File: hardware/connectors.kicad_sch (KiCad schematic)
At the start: 14 parts, among them J2 USB_C_Receptacle_USB2.0_16P, J3 Conn_01x03

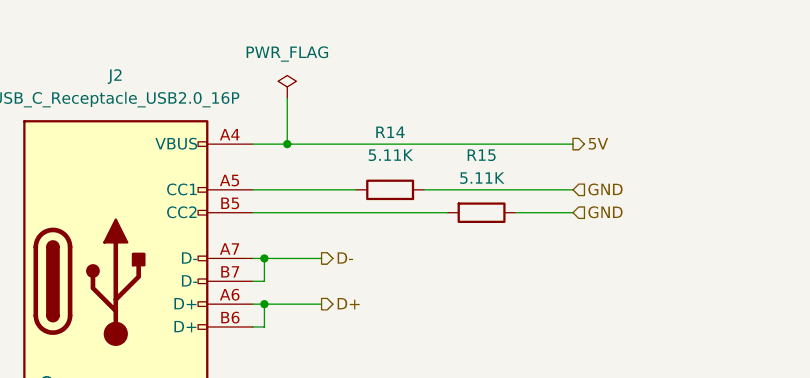
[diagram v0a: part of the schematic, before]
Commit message: Fix most of ERC on schema. Add missing wire on RV1. Add PWR_FLG on GND to avoid error. Add resistor for unused SPI_OUT of HV5622. Add PTC on 3v3 supply.
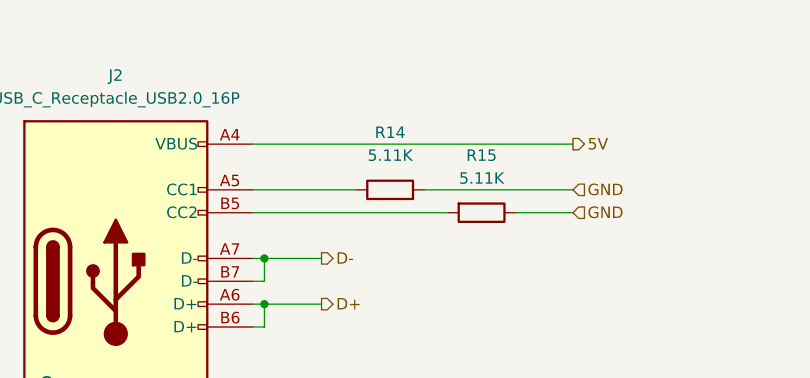
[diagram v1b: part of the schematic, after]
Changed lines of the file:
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@@
-	)
-	(junction
-		(at 80.01 44.45)
-		(diameter 0)
-		(color 0 0 0 0)
 	)
 	(junction
@@
 	(wire
 		(pts
-			(xy 80.01 39.37) (xy 80.01 44.45)
-		)
-		(stroke
-			(width 0)
-			(type default)
-		)
-	)
-	(wire
-		(pts
 			(xy 95.25 49.53) (xy 111.76 49.53)
 		)
@@
 	(wire
 		(pts
-			(xy 80.01 44.45) (xy 111.76 44.45)
+			(xy 76.2 44.45) (xy 111.76 44.45)
 		)
 		(stroke
@@
 		(pts
 			(xy 78.74 74.93) (xy 78.74 77.47)
-		)
-		(stroke
-			(width 0)
-			(type default)
-		)
-	)
-	(wire
-		(pts
-			(xy 76.2 44.45) (xy 80.01 44.45)
 		)
 		(stroke
@@
 					(unit 1)
 				)
-			)
-		)
-	)
-	(symbol
-		(lib_id "power:PWR_FLAG")
-		(at 80.01 39.37 0)
-		(unit 1)
-		(exclude_from_sim no)
-		(in_bom yes)
-		(on_board yes)
-		(dnp no)
-		(fields_autoplaced yes)
-		(property "Reference" "#FLG04"
-			(at 80.01 37.465 0)
-			(effects
-				(font
-					(size 1.27 1.27)
-				)
-				(hide yes)
-			)
-		)
-		(property "Value" "PWR_FLAG"
-			(at 80.01 34.29 0)
-			(effects
-				(font
-					(size 1.27 1.27)
-				)
-			)
-		)
-		(property "Footprint" ""
-			(at 80.01 39.37 0)
-			(effects
-				(font
-					(size 1.27 1.27)
-				)
-				(hide yes)
-			)
-		)
-		(property "Datasheet" "~"
-			(at 80.01 39.37 0)
-			(effects
-				(font
-					(size 1.27 1.27)
-				)
-				(hide yes)
-			)
-		)
-		(property "Description" "Special symbol for telling ERC where power comes from"
-			(at 80.01 39.37 0)
-			(effects
-				(font
-					(size 1.27 1.27)
-				)
-				(hide yes)
-			)
-		)
-		(pin "1"
-		)
-		(instances
-			(project ""
-				(path "/90430e5f-7049-4de8-b92d-f897c4a89819/7e2fbc03-0d09-4c94-a49f-ff5156ee2f2b"
-					(reference "#FLG04")
-					(unit 1)
-				)

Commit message: Update PCB.
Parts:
- added TH1, TH2: Thermistor_PTC, Resistor_SMD:R_1206_3216Metric, symbol Device:Thermistor_PTC
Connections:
- net 12V: now also TH1.1; no longer J3.3 (Pin_3)
- net 5V: now also TH2.1; no longer J2.A4 (VBUS), J2.A9 (VBUS), J2.B4 (VBUS), J2.B9 (VBUS)
- new net: J3.3 (Pin_3), TH1.2
- new net: J2.A4 (VBUS), J2.A9 (VBUS), J2.B4 (VBUS), J2.B9 (VBUS), TH2.2
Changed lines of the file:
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@@
 	(wire
 		(pts
-			(xy 199.39 43.18) (xy 212.09 43.18)
+			(xy 209.55 43.18) (xy 212.09 43.18)
+		)
+		(stroke
+			(width 0)
+			(type default)
+		)
+	)
+	(wire
+		(pts
+			(xy 199.39 50.8) (xy 200.66 50.8)
 		)
 		(stroke
@@
 	(wire
 		(pts
-			(xy 168.91 38.1) (xy 177.8 38.1)
+			(xy 208.28 50.8) (xy 209.55 50.8)
+		)
+		(stroke
+			(width 0)
+			(type default)
+		)
+	)
+	(wire
+		(pts
+			(xy 152.4 40.64) (xy 173.99 40.64)
+		)
+		(stroke
+			(width 0)
+			(type default)
+		)
+	)
+	(wire
+		(pts
+			(xy 152.4 38.1) (xy 177.8 38.1)
 		)
 		(stroke
@@
 	(wire
 		(pts
-			(xy 168.91 40.64) (xy 173.99 40.64)
-		)
-		(stroke
-			(width 0)
-			(type default)
-		)
-	)
-	(wire
-		(pts
 			(xy 76.2 64.77) (xy 77.47 64.77)
 		)
@@
 	(wire
 		(pts
-			(xy 76.2 44.45) (xy 111.76 44.45)
-		)
-		(stroke
-			(width 0)
-			(type default)
-		)
-	)
-	(wire
-		(pts
 			(xy 77.47 64.77) (xy 77.47 62.23)
 		)
@@
 	(wire
 		(pts
-			(xy 199.39 40.64) (xy 199.39 43.18)
+			(xy 199.39 40.64) (xy 199.39 50.8)
 		)
 		(stroke
@@
 	(wire
 		(pts
+			(xy 76.2 44.45) (xy 101.6 44.45)
+		)
+		(stroke
+			(width 0)
+			(type default)
+		)
+	)
+	(wire
+		(pts
 			(xy 78.74 74.93) (xy 78.74 77.47)
 		)
@@
 	(wire
 		(pts
+			(xy 209.55 50.8) (xy 209.55 43.18)
+		)
+		(stroke
+			(width 0)
+			(type default)
+		)
+	)
+	(wire
+		(pts
 			(xy 45.72 129.54) (xy 76.2 129.54)
+		)
+		(stroke
+			(width 0)
+			(type default)
+		)
+	)
+	(wire
+		(pts
+			(xy 109.22 44.45) (xy 111.76 44.45)
 		)
 		(stroke
@@
 		)
 	)
+	(hierarchical_label "5V"
+		(shape output)
+		(at 111.76 44.45 0)
+		(effects
+			(font
+				(size 1.27 1.27)
+			)
+			(justify left)
+		)
+	)
 	(hierarchical_label "GND"
 		(shape input)
@@
 		)
 	)
-	(hierarchical_label "5V"
-		(shape output)
-		(at 111.76 44.45 0)
-		(effects
-			(font
-				(size 1.27 1.27)
-			)
-			(justify left)
-		)
-	)
 	(hierarchical_label "D-"
 		(shape output)
@@
 	(hierarchical_label "170V"
 		(shape output)
-		(at 168.91 38.1 180)
+		(at 152.4 38.1 180)
 		(effects
 			(font
@@
 	(hierarchical_label "12V"
 		(shape output)
-		(at 168.91 40.64 180)
+		(at 152.4 40.64 180)
 		(effects
 			(font
@@
 		(on_board yes)
 		(dnp no)
-		(fields_autoplaced yes)
 		(property "Reference" "R14"
-			(at 91.44 43.18 90)
+			(at 91.44 47.244 90)
 			(effects
 				(font
@@
 		)
 		(property "Value" "5.11K"
-			(at 91.44 45.72 90)
+			(at 97.282 47.244 90)
 			(effects
 				(font
@@
 	)
 	(symbol
+		(lib_id "Device:Thermistor_PTC")
+		(at 105.41 44.45 270)
+		(unit 1)
+		(exclude_from_sim no)
+		(in_bom yes)
+		(on_board yes)
+		(dnp no)
+		(property "Reference" "TH2"
+			(at 105.41 39.878 90)
+			(effects
+				(font
+					(size 1.27 1.27)
+				)
+				(justify right)
+			)
+		)
+		(property "Value" "Thermistor_PTC"
+			(at 116.332 37.084 90)
+			(effects
+				(font
+					(size 1.27 1.27)
+				)
+				(justify right)
+			)
+		)
+		(property "Footprint" "Resistor_SMD:R_1206_3216Metric"
+			(at 100.33 45.72 0)
+			(effects
+				(font
+					(size 1.27 1.27)
+				)
+				(justify left)
+				(hide yes)
+			)
+		)
+		(property "Datasheet" "~"
+			(at 105.41 44.45 0)
+			(effects
+				(font
+					(size 1.27 1.27)
+				)
+				(hide yes)
+			)
+		)
+		(property "Description" "Temperature dependent resistor, positive temperature coefficient"
+			(at 105.41 44.45 0)
+			(effects
+				(font
+					(size 1.27 1.27)
+				)
+				(hide yes)
+			)
+		)
+		(pin "2"
+		)
+		(pin "1"
+		)
+		(instances
+			(project "nixie_clock"
+				(path "/90430e5f-7049-4de8-b92d-f897c4a89819/7e2fbc03-0d09-4c94-a49f-ff5156ee2f2b"
+					(reference "TH2")
+					(unit 1)
+				)
+			)
+		)
+	)
+	(symbol
 		(lib_id "Device:C")
 		(at 189.23 46.99 0)
@@
 		(on_board yes)
 		(dnp no)
-		(fields_autoplaced yes)
 		(property "Reference" "R15"
-			(at 101.6 45.72 90)
+			(at 101.6 54.864 90)
 			(effects
 				(font
@@
 		)
 		(property "Value" "5.11K"
-			(at 101.6 48.26 90)
+			(at 101.6 56.896 90)
 			(effects
 				(font
@@
 					(unit 1)
 				)
+			)
+		)
+	)
+	(symbol
+		(lib_id "Device:Thermistor_PTC")
+		(at 204.47 50.8 90)
+		(unit 1)
+		(exclude_from_sim no)
+		(in_bom yes)
+		(on_board yes)
+		(dnp no)
+		(property "Reference" "TH1"
+			(at 204.47 47.498 90)
+			(effects
+				(font
+					(size 1.27 1.27)
+				)
+				(justify right)
+			)
+		)
+		(property "Value" "Thermistor_PTC"
+			(at 198.374 45.466 90)
+			(effects
+				(font
+					(size 1.27 1.27)
+				)
+				(justify right)
+			)
+		)
+		(property "Footprint" "Resistor_SMD:R_1206_3216Metric"
+			(at 209.55 49.53 0)
+			(effects
+				(font
+					(size 1.27 1.27)
+				)
+				(justify left)
+				(hide yes)
+			)
+		)
+		(property "Datasheet" "~"
+			(at 204.47 50.8 0)
+			(effects
+				(font
+					(size 1.27 1.27)
+				)
+				(hide yes)
+			)
+		)
+		(property "Description" "Temperature dependent resistor, positive temperature coefficient"
+			(at 204.47 50.8 0)
+			(effects
+				(font
+					(size 1.27 1.27)
+				)
+				(hide yes)
+			)
+		)
+		(pin "2"
+		)
+		(pin "1"
+		)
+		(instances
+			(project "nixie_clock"
+				(path "/90430e5f-7049-4de8-b92d-f897c4a89819/7e2fbc03-0d09-4c94-a49f-ff5156ee2f2b"
+					(reference "TH1")
+					(unit 1)
+				)

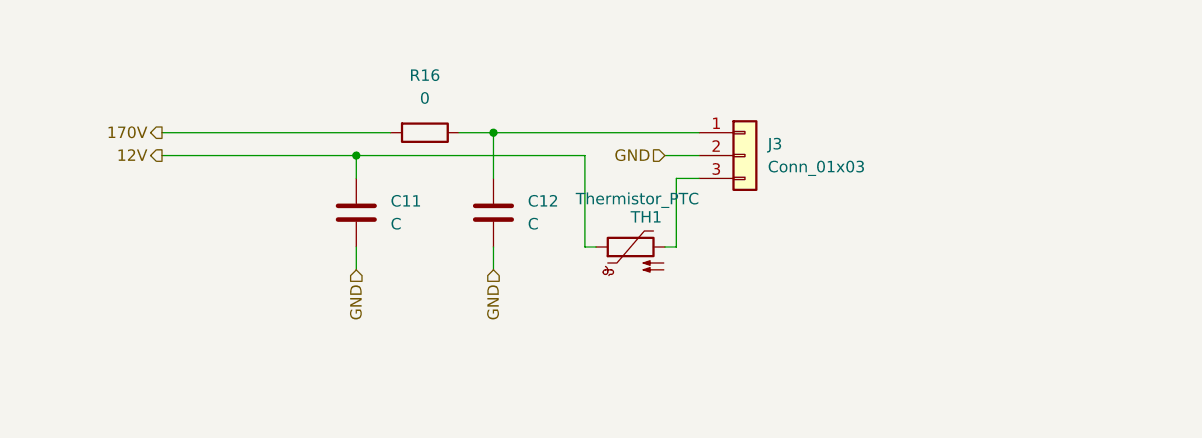
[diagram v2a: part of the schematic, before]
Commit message: Replace input with 12V barrel connector. Add test point for alternative 170V input.
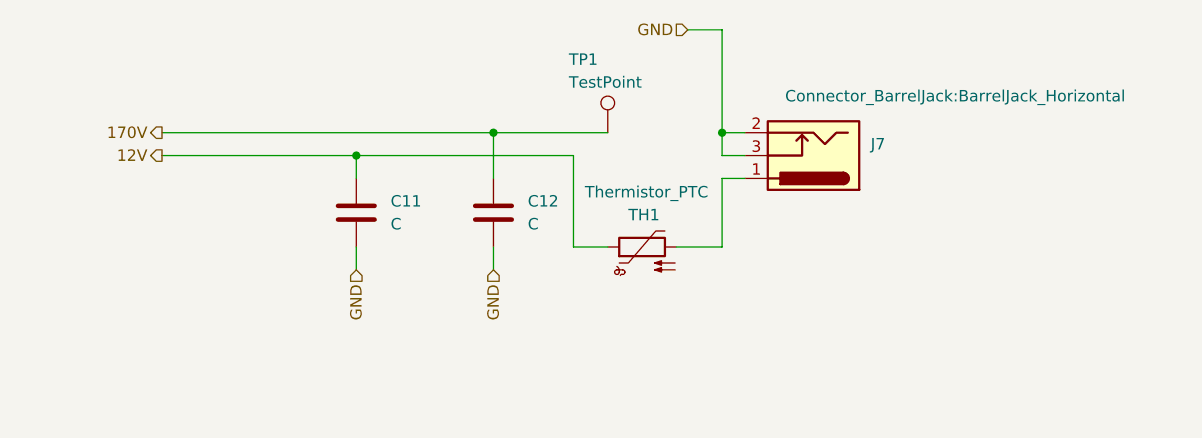
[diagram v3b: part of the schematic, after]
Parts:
- removed J3: Conn_01x03, TerminalBlock_Phoenix:TerminalBlock_Phoenix_PT-1,5-3-3.5-H_1x03_P3.50mm_Horizontal, symbol Connector_Generic:Conn_01x03
- removed R16: 0, Resistor_SMD:R_1206_3216Metric, symbol Device:R
- added J7: Barrel_Jack_Switch, Connector_BarrelJack:BarrelJack_Horizontal, symbol Connector:Barrel_Jack_Switch
- added TP1: TestPoint, TestPoint:TestPoint_Pad_D2.0mm, symbol Connector:TestPoint
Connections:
- net 170V: now also C12.1, TP1.1
- net GND: now also J7.2, J7.3
- net at TH1.2: now also J7.1
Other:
- moved on the sheet: TH1
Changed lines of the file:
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@@
+	)
+	(junction
+		(at 214.63 38.1)
+		(diameter 0)
+		(color 0 0 0 0)
 	)
 	(junction
@@
 	(wire
 		(pts
-			(xy 209.55 43.18) (xy 212.09 43.18)
-		)
-		(stroke
-			(width 0)
-			(type default)
-		)
-	)
-	(wire
-		(pts
-			(xy 199.39 50.8) (xy 200.66 50.8)
+			(xy 214.63 43.18) (xy 217.17 43.18)
+		)
+		(stroke
+			(width 0)
+			(type default)
+		)
+	)
+	(wire
+		(pts
+			(xy 198.12 50.8) (xy 201.93 50.8)
 		)
 		(stroke
@@
 	(wire
 		(pts
+			(xy 214.63 40.64) (xy 217.17 40.64)
+		)
+		(stroke
+			(width 0)
+			(type default)
+		)
+	)
+	(wire
+		(pts
 			(xy 104.14 129.54) (xy 127 129.54)
 		)
@@
 	(wire
 		(pts
-			(xy 185.42 38.1) (xy 189.23 38.1)
-		)
-		(stroke
-			(width 0)
-			(type default)
-		)
-	)
-	(wire
-		(pts
 			(xy 95.25 49.53) (xy 111.76 49.53)
 		)
@@
 	(wire
 		(pts
-			(xy 212.09 40.64) (xy 208.28 40.64)
+			(xy 214.63 26.67) (xy 210.82 26.67)
 		)
 		(stroke
@@
 	(wire
 		(pts
-			(xy 189.23 38.1) (xy 212.09 38.1)
-		)
-		(stroke
-			(width 0)
-			(type default)
-		)
-	)
-	(wire
-		(pts
-			(xy 208.28 50.8) (xy 209.55 50.8)
+			(xy 189.23 38.1) (xy 201.93 38.1)
+		)
+		(stroke
+			(width 0)
+			(type default)
+		)
+	)
+	(wire
+		(pts
+			(xy 209.55 50.8) (xy 214.63 50.8)
 		)
 		(stroke
@@
 	(wire
 		(pts
-			(xy 152.4 38.1) (xy 177.8 38.1)
+			(xy 152.4 38.1) (xy 189.23 38.1)
 		)
 		(stroke
@@
 	(wire
 		(pts
-			(xy 173.99 40.64) (xy 199.39 40.64)
+			(xy 173.99 40.64) (xy 198.12 40.64)
+		)
+		(stroke
+			(width 0)
+			(type default)
+		)
+	)
+	(wire
+		(pts
+			(xy 214.63 38.1) (xy 217.17 38.1)
 		)
 		(stroke
@@
 	(wire
 		(pts
-			(xy 199.39 40.64) (xy 199.39 50.8)
+			(xy 198.12 40.64) (xy 198.12 50.8)
 		)
 		(stroke
@@
 	(wire
 		(pts
-			(xy 209.55 50.8) (xy 209.55 43.18)
+			(xy 214.63 50.8) (xy 214.63 43.18)
+		)
+		(stroke
+			(width 0)
+			(type default)
+		)
+	)
+	(wire
+		(pts
+			(xy 214.63 38.1) (xy 214.63 40.64)
+		)
+		(stroke
+			(width 0)
+			(type default)
+		)
+	)
+	(wire
+		(pts
+			(xy 214.63 26.67) (xy 214.63 38.1)
 		)
 		(stroke
@@
 	(hierarchical_label "GND"
 		(shape input)
-		(at 208.28 40.64 180)
+		(at 210.82 26.67 180)
 		(effects
 			(font
@@
 			)
 			(justify right)
-		)
-	)
-	(symbol
-		(lib_id "Device:R")
-		(at 181.61 38.1 270)
-		(unit 1)
-		(exclude_from_sim no)
-		(in_bom yes)
-		(on_board yes)
-		(dnp no)
-		(fields_autoplaced yes)
-		(property "Reference" "R16"
-			(at 181.61 31.75 90)
-			(effects
-				(font
-					(size 1.27 1.27)
-				)
-			)
-		)
-		(property "Value" "0"
-			(at 181.61 34.29 90)
-			(effects
-				(font
-					(size 1.27 1.27)
-				)
-			)
-		)
-		(property "Footprint" "Resistor_SMD:R_1206_3216Metric"
-			(at 181.61 36.322 90)
-			(effects
-				(font
-					(size 1.27 1.27)
-				)
-				(hide yes)
-			)
-		)
-		(property "Datasheet" "~"
-			(at 181.61 38.1 0)
-			(effects
-				(font
-					(size 1.27 1.27)
-				)
-				(hide yes)
-			)
-		)
-		(property "Description" "Resistor"
-			(at 181.61 38.1 0)
-			(effects
-				(font
-					(size 1.27 1.27)
-				)
-				(hide yes)
-			)
-		)
-		(pin "1"
-		)
-		(pin "2"
-		)
-		(instances
-			(project "nixie_clock"
-				(path "/90430e5f-7049-4de8-b92d-f897c4a89819/7e2fbc03-0d09-4c94-a49f-ff5156ee2f2b"
-					(reference "R16")
-					(unit 1)
-				)
-			)
 		)
 	)
@@
 	)
 	(symbol
-		(lib_id "Connector_Generic:Conn_01x03")
-		(at 217.17 40.64 0)
+		(lib_id "Connector:TestPoint")
+		(at 201.93 38.1 0)
 		(unit 1)
 		(exclude_from_sim no)
@@
 		(on_board yes)
 		(dnp no)
-		(fields_autoplaced yes)
-		(property "Reference" "J3"
-			(at 219.71 39.3699 0)
-			(effects
-				(font
-					(size 1.27 1.27)
-				)
-				(justify left)
-			)
-		)
-		(property "Value" "Conn_01x03"
-			(at 219.71 41.9099 0)
-			(effects
-				(font
-					(size 1.27 1.27)
-				)
-				(justify left)
-			)
-		)
-		(property "Footprint" "TerminalBlock_Phoenix:TerminalBlock_Phoenix_PT-1,5-3-3.5-H_1x03_P3.50mm_Horizontal"
-			(at 217.17 40.64 0)
+		(property "Reference" "TP1"
+			(at 197.612 29.972 0)
+			(effects
+				(font
+					(size 1.27 1.27)
+				)
+				(justify left)
+			)
+		)
+		(property "Value" "TestPoint"
+			(at 197.612 32.512 0)
+			(effects
+				(font
+					(size 1.27 1.27)
+				)
+				(justify left)
+			)
+		)
+		(property "Footprint" "TestPoint:TestPoint_Pad_D2.0mm"
+			(at 207.01 38.1 0)
 			(effects
 				(font
@@
 		)
 		(property "Datasheet" "~"
-			(at 217.17 40.64 0)
-			(effects
-				(font
-					(size 1.27 1.27)
-				)
-				(hide yes)
-			)
-		)
-		(property "Description" "Generic connector, single row, 01x03, script generated (kicad-library-utils/schlib/autogen/connector/)"
-			(at 217.17 40.64 0)
+			(at 207.01 38.1 0)
+			(effects
+				(font
+					(size 1.27 1.27)
+				)
+				(hide yes)
+			)
+		)
+		(property "Description" "test point"
+			(at 201.93 38.1 0)
 			(effects
 				(font
@@
 		)
 		(pin "1"
-		)
-		(pin "2"
-		)
-		(pin "3"
 		)
 		(instances
 			(project ""
 				(path "/90430e5f-7049-4de8-b92d-f897c4a89819/7e2fbc03-0d09-4c94-a49f-ff5156ee2f2b"
-					(reference "J3")
+					(reference "TP1")
 					(unit 1)
 				)
@@
 	)
 	(symbol
+		(lib_id "Connector:Barrel_Jack_Switch")
+		(at 224.79 40.64 180)
+		(unit 1)
+		(exclude_from_sim no)
+		(in_bom yes)
+		(on_board yes)
+		(dnp no)
+		(property "Reference" "J7"
+			(at 231.14 39.3699 0)
+			(effects
+				(font
+					(size 1.27 1.27)
+				)
+				(justify right)
+			)
+		)
+		(property "Value" "Barrel_Jack_Switch"
+			(at 231.14 41.9099 0)
+			(effects
+				(font
+					(size 1.27 1.27)
+				)
+				(justify right)
+				(hide yes)
+			)
+		)
+		(property "Footprint" "Connector_BarrelJack:BarrelJack_Horizontal"
+			(at 240.538 34.036 0)
+			(effects
+				(font
+					(size 1.27 1.27)
+				)
+			)
+		)
+		(property "Datasheet" "~"
+			(at 223.52 39.624 0)
+			(effects
+				(font
+					(size 1.27 1.27)
+				)
+				(hide yes)
+			)
+		)
+		(property "Description" "DC Barrel Jack with an internal switch"
+			(at 224.79 40.64 0)
+			(effects
+				(font
+					(size 1.27 1.27)
+				)
+				(hide yes)
+			)
+		)
+		(pin "1"
+		)
+		(pin "3"
+		)
+		(pin "2"
+		)
+		(instances
+			(project ""
+				(path "/90430e5f-7049-4de8-b92d-f897c4a89819/7e2fbc03-0d09-4c94-a49f-ff5156ee2f2b"
+					(reference "J7")
+					(unit 1)
+				)
+			)
+		)
+	)
+	(symbol
 		(lib_id "Device:R")
 		(at 87.63 81.28 0)
@@
 	(symbol
 		(lib_id "Device:Thermistor_PTC")
-		(at 204.47 50.8 90)
+		(at 205.74 50.8 90)
 		(unit 1)
 		(exclude_from_sim no)
@@
 		(dnp no)
 		(property "Reference" "TH1"
-			(at 204.47 47.498 90)
+			(at 204.216 47.244 90)
 			(effects
 				(font
@@
 		)
 		(property "Value" "Thermistor_PTC"
-			(at 198.374 45.466 90)
+			(at 199.39 44.704 90)
 			(effects
 				(font
@@
 		)
 		(property "Footprint" "Resistor_SMD:R_1206_3216Metric"
-			(at 209.55 49.53 0)
+			(at 210.82 49.53 0)
 			(effects
 				(font
@@
 		)
 		(property "Datasheet" "~"
-			(at 204.47 50.8 0)
+			(at 205.74 50.8 0)
 			(effects
 				(font
@@
 		)
 		(property "Description" "Temperature dependent resistor, positive temperature coefficient"
-			(at 204.47 50.8 0)
-			(effects
-				(font
+			(at 205.74 50.8 0)
+			(effects
+				(font
